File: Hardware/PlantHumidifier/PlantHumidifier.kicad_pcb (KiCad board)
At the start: 2 copper layers, 8 parts, among them J1 110990030, J2 Conn_01x05_Female, J3 Conn_01x04_Female, J4 Conn_01x04_Female, U1 WeMos_D1_mini

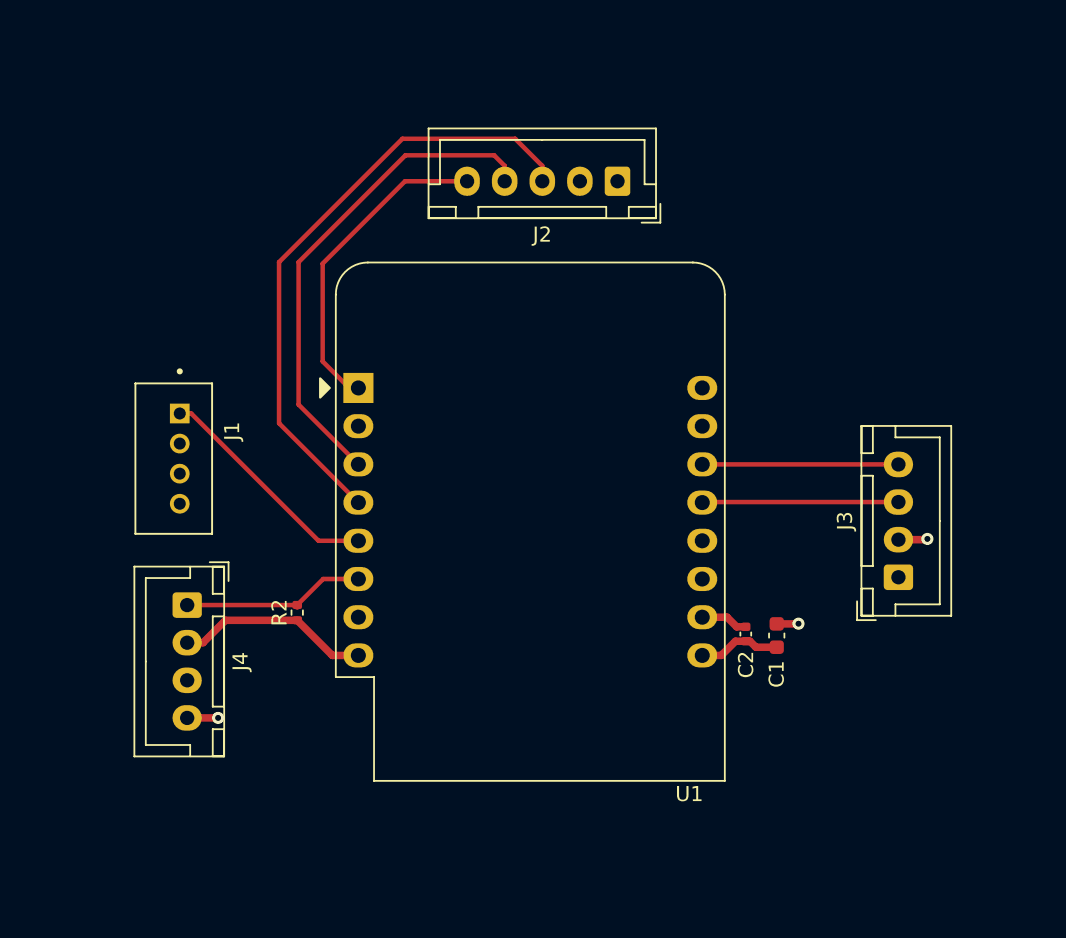
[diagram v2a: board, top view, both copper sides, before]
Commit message: Layout: Route power and ground rails
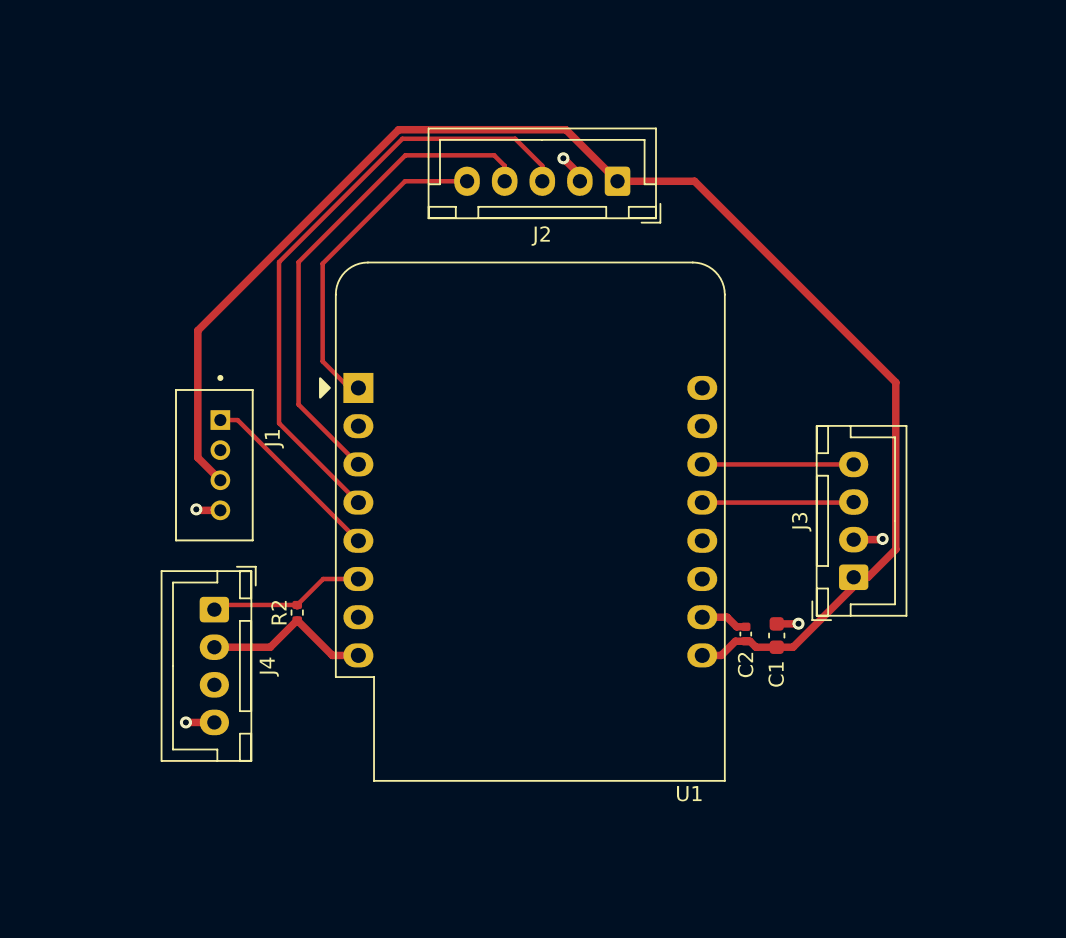
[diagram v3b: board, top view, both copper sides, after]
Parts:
- moved J3 2.97 mm to (110.5, 88.2)
- moved J1 2.74 mm to (68.4, 80.7)
- moved J4 1.83 mm to (68.0, 90.3)
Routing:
- net +5V: track 5.78 -> 97.0 mm
- net GND: track 8.67 -> 12.1 mm, vias 3 -> 5
- net /OLED_SCL: track 13.0 -> 10.1 mm
- net /OLED_SDA: track 13.1 -> 10.1 mm
- net /Atomizer: track 15.4 -> 12.5 mm
- net +3V3: track 13.0 -> 11.3 mm
- net /DHT22_Sense: track 12.3 -> 10.7 mm
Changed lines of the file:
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@@
   )
   (footprint "Connector_JST:JST_XH_B4B-XH-A_1x04_P2.50mm_Vertical" (layer "F.Cu")
-    (at 66.1924 90 -90)
+    (at 68 90.3 -90)
     (descr "JST XH series connector, B4B-XH-A (http://www.jst-mfg.com/product/pdf/eng/eXH.pdf), generated with kicad-footprint-generator")
     (tags "connector JST XH vertical")
@@
   )
   (footprint "Connector_JST:JST_XH_B4B-XH-A_1x04_P2.50mm_Vertical" (layer "F.Cu")
-    (at 113.475 88.15 90)
+    (at 110.5 88.15 90)
     (descr "JST XH series connector, B4B-XH-A (http://www.jst-mfg.com/product/pdf/eng/eXH.pdf), generated with kicad-footprint-generator")
     (tags "connector JST XH vertical")
@@
   )
   (footprint "Seeed_Connectors:SEEED_110990030" (layer "F.Cu")
-    (at 65.7 80.2625 -90)
+    (at 68.4 80.7 -90)
     (property "MANUFACTURER" "Seeed Technology")
     (property "MAXIMUM_PACKAGE_HEIGHT" "8.1mm")
@@
       (effects (font (size 1 1) (thickness 0.15)))
     )
-    (fp_text value "110990030" (at 4.525 4.385 90) (layer "F.Fab")
+    (fp_text value "110990030" (at 4.825 2.5774 90) (layer "F.Fab")
       (effects (font (size 1 1) (thickness 0.15)))
     )
@@
   )
   (segment (start 103.3272 92.4026) (end 103.604 92.4026) (width 0.5) (layer "F.Cu") (net 1))
+  (segment (start 66.9 80.2) (end 66.9 71.751472) (width 0.5) (layer "F.Cu") (net 1))
+  (segment (start 66.9 71.751472) (end 80.251472 58.4) (width 0.5) (layer "F.Cu") (net 1))
+  (segment (start 106.472082 92.7992) (end 105.3846 92.7992) (width 0.5) (layer "F.Cu") (net 1))
   (segment (start 104.0006 92.7992) (end 105.3846 92.7992) (width 0.5) (layer "F.Cu") (net 1))
   (segment (start 103.604 92.4026) (end 104.0006 92.7992) (width 0.5) (layer "F.Cu") (net 1))
   (segment (start 102.644 92.4026) (end 103.3272 92.4026) (width 0.5) (layer "F.Cu") (net 1))
-  (segment (start 113.475 88.15) (end 113.475 88.425) (width 0.5) (layer "F.Cu") (net 1))
+  (segment (start 68.4 81.7) (end 66.9 80.2) (width 0.5) (layer "F.Cu") (net 1))
+  (segment (start 113.3 86.3) (end 113.3 75.2) (width 0.5) (layer "F.Cu") (net 1))
+  (segment (start 94.8 61.825) (end 99.925 61.825) (width 0.5) (layer "F.Cu") (net 1))
+  (segment (start 80.251472 58.4) (end 91.375 58.4) (width 0.5) (layer "F.Cu") (net 1))
+  (segment (start 110.5 88.771282) (end 106.472082 92.7992) (width 0.5) (layer "F.Cu") (net 1))
   (segment (start 101.7016 93.345) (end 102.644 92.4026) (width 0.5) (layer "F.Cu") (net 1))
+  (segment (start 113.3 75.2) (end 99.925 61.825) (width 0.5) (layer "F.Cu") (net 1))
+  (segment (start 91.375 58.4) (end 94.8 61.825) (width 0.5) (layer "F.Cu") (net 1))
+  (segment (start 111.45 88.15) (end 113.3 86.3) (width 0.5) (layer "F.Cu") (net 1))
+  (segment (start 110.5 88.15) (end 111.45 88.15) (width 0.5) (layer "F.Cu") (net 1))
+  (segment (start 110.5 88.15) (end 110.5 88.771282) (width 0.5) (layer "F.Cu") (net 1))
   (segment (start 100.434 93.345) (end 101.7016 93.345) (width 0.5) (layer "F.Cu") (net 1))
-  (segment (start 66.1924 97.5) (end 68.25 97.5) (width 0.5) (layer "F.Cu") (net 2))
+  (segment (start 66.8625 83.7) (end 66.8 83.6375) (width 0.5) (layer "F.Cu") (net 2))
   (segment (start 106.82 91.2492) (end 106.8324 91.2368) (width 0.5) (layer "F.Cu") (net 2))
   (segment (start 105.3468 91.2114) (end 105.3846 91.2492) (width 0.5) (layer "F.Cu") (net 2))
   (segment (start 100.434 90.805) (end 102.0826 90.805) (width 0.5) (layer "F.Cu") (net 2))
   (segment (start 105.3846 91.2492) (end 106.82 91.2492) (width 0.5) (layer "F.Cu") (net 2))
-  (segment (start 113.475 85.65) (end 115.35 85.65) (width 0.5) (layer "F.Cu") (net 2))
+  (segment (start 110.5 85.65) (end 112.375 85.65) (width 0.5) (layer "F.Cu") (net 2))
+  (segment (start 68 97.8) (end 66.1076 97.8) (width 0.5) (layer "F.Cu") (net 2))
   (segment (start 102.0826 90.805) (end 102.7202 91.4426) (width 0.5) (layer "F.Cu") (net 2))
+  (segment (start 68.4 83.7) (end 66.8625 83.7) (width 0.5) (layer "F.Cu") (net 2))
   (segment (start 102.7202 91.4426) (end 103.3272 91.4426) (width 0.5) (layer "F.Cu") (net 2))
-  (segment (start 115.35 85.65) (end 115.4 85.6) (width 0.5) (layer "F.Cu") (net 2))
-  (via (at 68.25 97.5) (size 0.8) (drill 0.4) (layers "F.Cu" "B.Cu") (net 2))
+  (segment (start 92.3 61.825) (end 92.3 61.4) (width 0.5) (layer "F.Cu") (net 2))
+  (segment (start 112.375 85.65) (end 112.425 85.6) (width 0.5) (layer "F.Cu") (net 2))
+  (segment (start 92.3 61.4) (end 91.2 60.3) (width 0.5) (layer "F.Cu") (net 2))
+  (via (at 66.8 83.6375) (size 0.8) (drill 0.4) (layers "F.Cu" "B.Cu") (net 2))
+  (via (at 66.1076 97.8) (size 0.8) (drill 0.4) (layers "F.Cu" "B.Cu") (net 2))
+  (via (at 91.2 60.3) (size 0.8) (drill 0.4) (layers "F.Cu" "B.Cu") (net 2))
   (via (at 106.8324 91.2368) (size 0.8) (drill 0.4) (layers "F.Cu" "B.Cu") (net 2))
-  (via (at 115.4 85.6) (size 0.8) (drill 0.4) (layers "F.Cu" "B.Cu") (net 2))
-  (segment (start 65.7 77.2625) (end 66.4625 77.2625) (width 0.3) (layer "F.Cu") (net 3))
-  (segment (start 66.4625 77.2625) (end 74.925 85.725) (width 0.3) (layer "F.Cu") (net 3))
-  (segment (start 74.925 85.725) (end 77.574 85.725) (width 0.3) (layer "F.Cu") (net 3))
+  (via (at 112.425 85.6) (size 0.8) (drill 0.4) (layers "F.Cu" "B.Cu") (net 2))
+  (segment (start 69.549 77.7) (end 77.574 85.725) (width 0.3) (layer "F.Cu") (net 3))
+  (segment (start 68.4 77.7) (end 69.549 77.7) (width 0.3) (layer "F.Cu") (net 3))
+  (segment (start 110.465 83.185) (end 110.5 83.15) (width 0.3) (layer "F.Cu") (net 5))
   (segment (start 100.469 83.15) (end 100.434 83.185) (width 0.3) (layer "F.Cu") (net 5))
-  (segment (start 113.475 83.15) (end 100.469 83.15) (width 0.3) (layer "F.Cu") (net 5))
-  (segment (start 113.47 80.645) (end 113.475 80.65) (width 0.3) (layer "F.Cu") (net 6))
-  (segment (start 100.434 80.645) (end 113.47 80.645) (width 0.3) (layer "F.Cu") (net 6))
+  (segment (start 100.434 83.185) (end 110.465 83.185) (width 0.3) (layer "F.Cu") (net 5))
+  (segment (start 110.495 80.645) (end 110.5 80.65) (width 0.3) (layer "F.Cu") (net 6))
+  (segment (start 100.439 80.65) (end 100.434 80.645) (width 0.3) (layer "F.Cu") (net 6))
+  (segment (start 110.5 80.65) (end 100.439 80.65) (width 0.3) (layer "F.Cu") (net 6))
   (segment (start 72.3 77.911) (end 77.574 83.185) (width 0.3) (layer "F.Cu") (net 7))
   (segment (start 80.5 59) (end 72.3 67.2) (width 0.3) (layer "F.Cu") (net 7))
@@
   (segment (start 80.7 60.1) (end 73.6 67.2) (width 0.3) (layer "F.Cu") (net 8))
   (segment (start 86.6 60.1) (end 80.7 60.1) (width 0.3) (layer "F.Cu") (net 8))
-  (segment (start 68.74 91.01) (end 73.5076 91.01) (width 0.5) (layer "F.Cu") (net 10))
+  (segment (start 68 92.8) (end 71.7176 92.8) (width 0.5) (layer "F.Cu") (net 10))
   (segment (start 73.5076 91.01) (end 75.8426 93.345) (width 0.5) (layer "F.Cu") (net 10))
   (segment (start 75.8426 93.345) (end 77.574 93.345) (width 0.5) (layer "F.Cu") (net 10))
-  (segment (start 67.25 92.5) (end 68.74 91.01) (width 0.5) (layer "F.Cu") (net 10))
-  (segment (start 66.1924 92.5) (end 67.25 92.5) (width 0.5) (layer "F.Cu") (net 10))
+  (segment (start 71.7176 92.8) (end 73.5076 91.01) (width 0.5) (layer "F.Cu") (net 10))
+  (segment (start 68.31 89.99) (end 68 90.3) (width 0.3) (layer "F.Cu") (net 11))
   (segment (start 73.4976 90) (end 73.5076 89.99) (width 0.3) (layer "F.Cu") (net 11))
   (segment (start 73.5076 89.99) (end 75.2326 88.265) (width 0.3) (layer "F.Cu") (net 11))
   (segment (start 75.2326 88.265) (end 77.574 88.265) (width 0.3) (layer "F.Cu") (net 11))
-  (segment (start 66.1924 90) (end 73.4976 90) (width 0.3) (layer "F.Cu") (net 11))
+  (segment (start 73.5076 89.99) (end 68.31 89.99) (width 0.3) (layer "F.Cu") (net 11))
   (segment (start 73.3396 90) (end 73.5076 90.168) (width 0.3) (layer "F.Cu") (net 11))
   (segment (start 76.965 75.565) (end 77.574 75.565) (width 0.3) (layer "F.Cu") (net 14))

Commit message: Layout: Make edge cuts
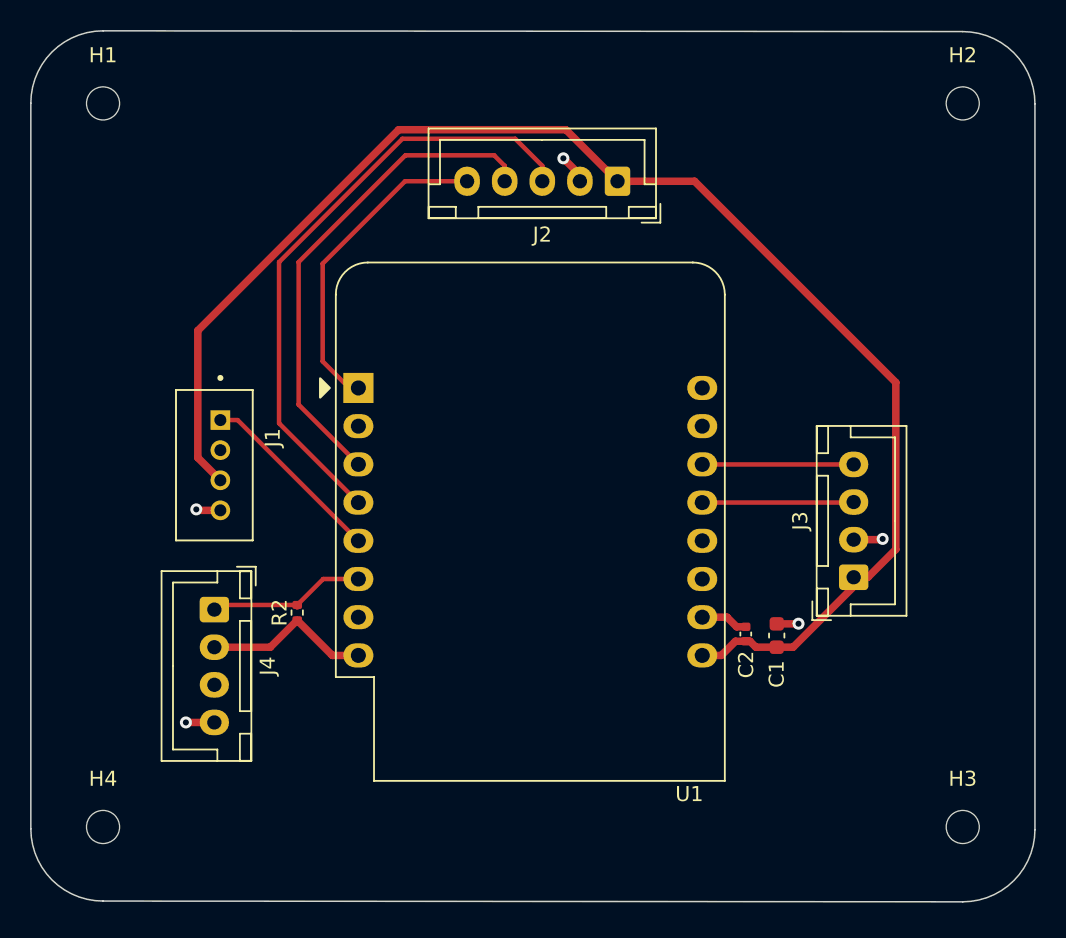
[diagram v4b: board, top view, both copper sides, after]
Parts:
- added H1: MountingHole, MountingHole:MountingHole_2.2mm_M2, F.Cu at (60.6, 56.6)
- added H2: MountingHole, MountingHole:MountingHole_2.2mm_M2, F.Cu at (117.8, 56.6)
- added H3: MountingHole, MountingHole:MountingHole_2.2mm_M2, F.Cu at (117.8, 104.8)
- added H4: MountingHole, MountingHole:MountingHole_2.2mm_M2, F.Cu at (60.6, 104.8)
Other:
- board outline added: 66.8 x 57.9 mm
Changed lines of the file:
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@@
   (net 17 "unconnected-(U1-Pad15)")
   (net 18 "unconnected-(U1-Pad16)")
+  (footprint "MountingHole:MountingHole_2.2mm_M2" (layer "F.Cu")
+    (at 60.6 104.75)
+    (descr "Mounting Hole 2.2mm, no annular, M2")
+    (tags "mounting hole 2.2mm no annular m2")
+    (property "Sheetfile" "PlantHumidifier.kicad_sch")
+    (property "Sheetname" "")
+    (attr exclude_from_pos_files)
+    (fp_text reference "H4" (at 0 -3.2) (layer "F.SilkS")
+      (effects (font (size 1 1) (thickness 0.15)))
+    )
+    (fp_text value "MountingHole" (at 0 3.2) (layer "F.Fab")
+      (effects (font (size 1 1) (thickness 0.15)))
+    )
+    (fp_text user "${REFERENCE}" (at 0 0) (layer "F.Fab")
+      (effects (font (size 1 1) (thickness 0.15)))
+    )
+    (fp_circle (center 0 0) (end 2.2 0) (layer "Cmts.User") (width 0.15) (fill none))
+    (fp_circle (center 0 0) (end 2.45 0) (layer "F.CrtYd") (width 0.05) (fill none))
+    (pad "" np_thru_hole circle (at 0 0) (size 2.2 2.2) (drill 2.2) (layers *.Cu *.Mask))
+  )
   (footprint "Connector_JST:JST_XH_B5B-XH-A_1x05_P2.50mm_Vertical" (layer "F.Cu")
     (at 94.8 61.825 180)
@@
     )
   )
+  (footprint "MountingHole:MountingHole_2.2mm_M2" (layer "F.Cu")
+    (at 117.75 104.75)
+    (descr "Mounting Hole 2.2mm, no annular, M2")
+    (tags "mounting hole 2.2mm no annular m2")
+    (property "Sheetfile" "PlantHumidifier.kicad_sch")
+    (property "Sheetname" "")
+    (attr exclude_from_pos_files)
+    (fp_text reference "H3" (at 0 -3.2) (layer "F.SilkS")
+      (effects (font (size 1 1) (thickness 0.15)))
+    )
+    (fp_text value "MountingHole" (at 0 3.2) (layer "F.Fab")
+      (effects (font (size 1 1) (thickness 0.15)))
+    )
+    (fp_text user "${REFERENCE}" (at 0 0) (layer "F.Fab")
+      (effects (font (size 1 1) (thickness 0.15)))
+    )
+    (fp_circle (center 0 0) (end 2.2 0) (layer "Cmts.User") (width 0.15) (fill none))
+    (fp_circle (center 0 0) (end 2.45 0) (layer "F.CrtYd") (width 0.05) (fill none))
+    (pad "" np_thru_hole circle (at 0 0) (size 2.2 2.2) (drill 2.2) (layers *.Cu *.Mask))
+  )
   (footprint "Resistor_SMD:R_0402_1005Metric" (layer "F.Cu")
     (at 73.5076 90.5 90)
@@
       (rotate (xyz 0 0 0))
     )
+  )
+  (footprint "MountingHole:MountingHole_2.2mm_M2" (layer "F.Cu")
+    (at 117.75 56.65)
+    (descr "Mounting Hole 2.2mm, no annular, M2")
+    (tags "mounting hole 2.2mm no annular m2")
+    (property "Sheetfile" "PlantHumidifier.kicad_sch")
+    (property "Sheetname" "")
+    (attr exclude_from_pos_files)
+    (fp_text reference "H2" (at 0 -3.2) (layer "F.SilkS")
+      (effects (font (size 1 1) (thickness 0.15)))
+    )
+    (fp_text value "MountingHole" (at 0 3.2) (layer "F.Fab")
+      (effects (font (size 1 1) (thickness 0.15)))
+    )
+    (fp_text user "${REFERENCE}" (at 0 0) (layer "F.Fab")
+      (effects (font (size 1 1) (thickness 0.15)))
+    )
+    (fp_circle (center 0 0) (end 2.2 0) (layer "Cmts.User") (width 0.15) (fill none))
+    (fp_circle (center 0 0) (end 2.45 0) (layer "F.CrtYd") (width 0.05) (fill none))
+    (pad "" np_thru_hole circle (at 0 0) (size 2.2 2.2) (drill 2.2) (layers *.Cu *.Mask))
+  )
+  (footprint "MountingHole:MountingHole_2.2mm_M2" (layer "F.Cu")
+    (at 60.6 56.65)
+    (descr "Mounting Hole 2.2mm, no annular, M2")
+    (tags "mounting hole 2.2mm no annular m2")
+    (property "Sheetfile" "PlantHumidifier.kicad_sch")
+    (property "Sheetname" "")
+    (attr exclude_from_pos_files)
+    (fp_text reference "H1" (at 0 -3.2) (layer "F.SilkS")
+      (effects (font (size 1 1) (thickness 0.15)))
+    )
+    (fp_text value "MountingHole" (at 0 3.2) (layer "F.Fab")
+      (effects (font (size 1 1) (thickness 0.15)))
+    )
+    (fp_text user "${REFERENCE}" (at 0 0) (layer "F.Fab")
+      (effects (font (size 1 1) (thickness 0.15)))
+    )
+    (fp_circle (center 0 0) (end 2.2 0) (layer "Cmts.User") (width 0.15) (fill none))
+    (fp_circle (center 0 0) (end 2.45 0) (layer "F.CrtYd") (width 0.05) (fill none))
+    (pad "" np_thru_hole circle (at 0 0) (size 2.2 2.2) (drill 2.2) (layers *.Cu *.Mask))
   )
   (footprint "Module:WEMOS_D1_mini_light" (layer "F.Cu")
@@
       (net 2 "GND") (pinfunction "4") (pintype "passive"))
   )
+  (gr_line (start 122.55 56.675) (end 122.55 104.925) (layer "Edge.Cuts") (width 0.1))
+  (gr_line (start 60.6 51.825) (end 117.75 51.875) (layer "Edge.Cuts") (width 0.1))
+  (gr_arc (start 55.8 56.625) (mid 57.205887 53.230887) (end 60.6 51.825) (layer "Edge.Cuts") (width 0.1))
+  (gr_line (start 60.6 109.675) (end 117.75 109.725) (layer "Edge.Cuts") (width 0.1))
+  (gr_line (start 55.8 56.625) (end 55.8 104.875) (layer "Edge.Cuts") (width 0.1))
+  (gr_arc (start 122.55 104.925) (mid 121.144113 108.319113) (end 117.75 109.725) (layer "Edge.Cuts") (width 0.1))
+  (gr_arc (start 60.6 109.675) (mid 57.205887 108.269113) (end 55.8 104.875) (layer "Edge.Cuts") (width 0.1))
+  (gr_arc (start 117.75 51.875) (mid 121.144113 53.280887) (end 122.55 56.675) (layer "Edge.Cuts") (width 0.1))
   (segment (start 103.3272 92.4026) (end 103.604 92.4026) (width 0.5) (layer "F.Cu") (net 1))
   (segment (start 66.9 80.2) (end 66.9 71.751472) (width 0.5) (layer "F.Cu") (net 1))

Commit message: Layout: Add copper pour
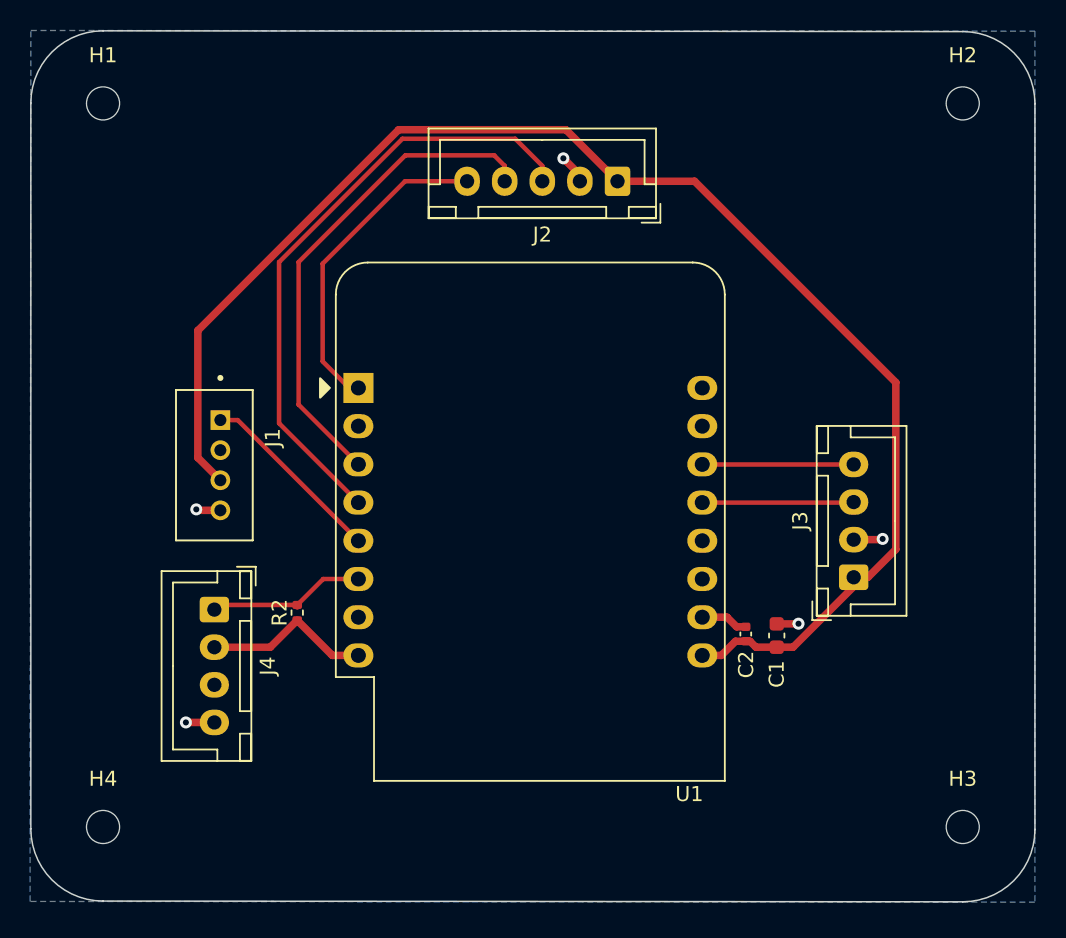
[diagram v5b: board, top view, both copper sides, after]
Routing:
- added copper zone on B.Cu, net GND
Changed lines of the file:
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@@
   (segment (start 80.675 61.825) (end 75.2 67.3) (width 0.3) (layer "F.Cu") (net 14))
   (segment (start 84.8 61.825) (end 80.675 61.825) (width 0.3) (layer "F.Cu") (net 14))
+  (zone (net 2) (net_name "GND") (layer "B.Cu") (hatch edge 0.508)
+    (connect_pads (clearance 0.3))
+    (min_thickness 0.25) (filled_areas_thickness no)
+    (fill (thermal_gap 0.5) (thermal_bridge_width 0.5))
+    (polygon
+      (pts
+        (xy 122.55 51.85)
+        (xy 122.55 109.75)
+        (xy 55.75 109.7)
+        (xy 55.8 51.8)
+      )
+    )
+  )
 )
